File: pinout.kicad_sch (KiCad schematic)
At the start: 2 parts, among them J4 Conn_01x14_Pin, J6 Conn_01x14_Pin

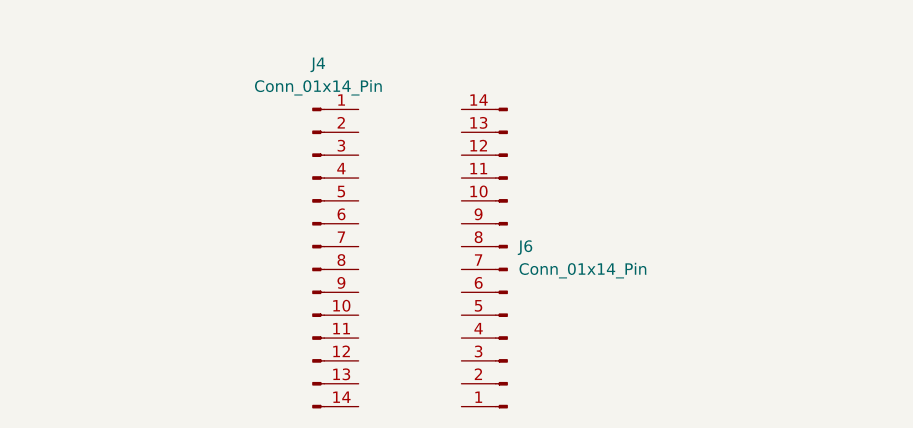
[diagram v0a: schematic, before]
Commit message: Added test Antenna
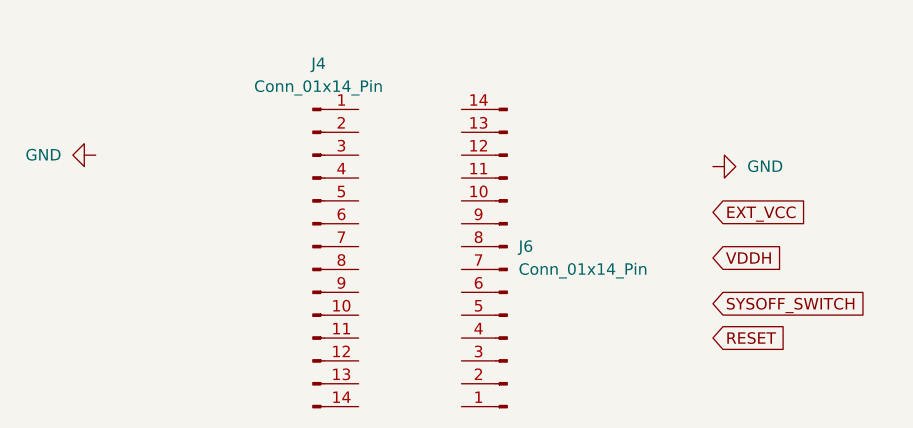
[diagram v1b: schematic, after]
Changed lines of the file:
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@@
 	(generator_version "9.0")
 	(paper "A4")
+	(global_label "EXT_VCC"
+		(shape input)
+		(at 157.48 96.52 0)
+		(fields_autoplaced yes)
+		(effects
+			(font
+				(size 1.27 1.27)
+			)
+			(justify left)
+		)
+		(property "Intersheetrefs" "${INTERSHEET_REFS}"
+			(at 168.3875 96.52 0)
+			(effects
+				(font
+					(size 1.27 1.27)
+				)
+				(justify left)
+				(hide yes)
+			)
+		)
+	)
+	(global_label "SYSOFF_SWITCH"
+		(shape input)
+		(at 157.48 106.68 0)
+		(fields_autoplaced yes)
+		(effects
+			(font
+				(size 1.27 1.27)
+			)
+			(justify left)
+		)
+		(property "Intersheetrefs" "${INTERSHEET_REFS}"
+			(at 175.2819 106.68 0)
+			(effects
+				(font
+					(size 1.27 1.27)
+				)
+				(justify left)
+				(hide yes)
+			)
+		)
+	)
+	(global_label "VDDH"
+		(shape input)
+		(at 157.48 101.6 0)
+		(fields_autoplaced yes)
+		(effects
+			(font
+				(size 1.27 1.27)
+			)
+			(justify left)
+		)
+		(property "Intersheetrefs" "${INTERSHEET_REFS}"
+			(at 165.4243 101.6 0)
+			(effects
+				(font
+					(size 1.27 1.27)
+				)
+				(justify left)
+				(hide yes)
+			)
+		)
+	)
+	(global_label "RESET"
+		(shape input)
+		(at 157.48 110.49 0)
+		(fields_autoplaced yes)
+		(effects
+			(font
+				(size 1.27 1.27)
+			)
+			(justify left)
+		)
+		(property "Intersheetrefs" "${INTERSHEET_REFS}"
+			(at 166.2103 110.49 0)
+			(effects
+				(font
+					(size 1.27 1.27)
+				)
+				(justify left)
+				(hide yes)
+			)
+		)
+	)
 	(symbol
 		(lib_id "Connector:Conn_01x14_Pin")
@@
 					(unit 1)
 				)
+			)
+		)
+	)
+	(symbol
+		(lib_id "power:GND")
+		(at 157.48 91.44 90)
+		(unit 1)
+		(exclude_from_sim no)
+		(in_bom yes)
+		(on_board yes)
+		(dnp no)
+		(fields_autoplaced yes)
+		(property "Reference" "#PWR038"
+			(at 163.83 91.44 0)
+			(effects
+				(font
+					(size 1.27 1.27)
+				)
+				(hide yes)
+			)
+		)
+		(property "Value" "GND"
+			(at 161.29 91.4399 90)
+			(effects
+				(font
+					(size 1.27 1.27)
+				)
+				(justify right)
+			)
+		)
+		(property "Footprint" ""
+			(at 157.48 91.44 0)
+			(effects
+				(font
+					(size 1.27 1.27)
+				)
+				(hide yes)
+			)
+		)
+		(property "Datasheet" ""
+			(at 157.48 91.44 0)
+			(effects
+				(font
+					(size 1.27 1.27)
+				)
+				(hide yes)
+			)
+		)
+		(property "Description" "Power symbol creates a global label with name \"GND\" , ground"
+			(at 157.48 91.44 0)
+			(effects
+				(font
+					(size 1.27 1.27)
+				)
+				(hide yes)
+			)
+		)
+		(pin "1"
+		)
+		(instances
+			(project "Slim Keyboard"
+				(path "/5d65a0d4-45a3-4af0-996a-c0381d04499a/f42a8a8a-4a34-440a-8e58-9c442fe0d23e/302a6436-4e3c-4497-ba91-0be99fe995f0"
+					(reference "#PWR038")
+					(unit 1)
+				)
+			)
+		)
+	)
+	(symbol
+		(lib_id "power:GND")
+		(at 88.9 90.17 270)
+		(unit 1)
+		(exclude_from_sim no)
+		(in_bom yes)
+		(on_board yes)
+		(dnp no)
+		(fields_autoplaced yes)
+		(property "Reference" "#PWR039"
+			(at 82.55 90.17 0)
+			(effects
+				(font
+					(size 1.27 1.27)
+				)
+				(hide yes)
+			)
+		)
+		(property "Value" "GND"
+			(at 85.09 90.1699 90)
+			(effects
+				(font
+					(size 1.27 1.27)
+				)
+				(justify right)
+			)
+		)
+		(property "Footprint" ""
+			(at 88.9 90.17 0)
+			(effects
+				(font
+					(size 1.27 1.27)
+				)
+				(hide yes)
+			)
+		)
+		(property "Datasheet" ""
+			(at 88.9 90.17 0)
+			(effects
+				(font
+					(size 1.27 1.27)
+				)
+				(hide yes)
+			)
+		)
+		(property "Description" "Power symbol creates a global label with name \"GND\" , ground"
+			(at 88.9 90.17 0)
+			(effects
+				(font
+					(size 1.27 1.27)
+				)
+				(hide yes)
+			)
+		)
+		(pin "1"
+		)
+		(instances
+			(project "Slim Keyboard"
+				(path "/5d65a0d4-45a3-4af0-996a-c0381d04499a/f42a8a8a-4a34-440a-8e58-9c442fe0d23e/302a6436-4e3c-4497-ba91-0be99fe995f0"
+					(reference "#PWR039")
+					(unit 1)
+				)

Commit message: Adjusted Footprint sizes
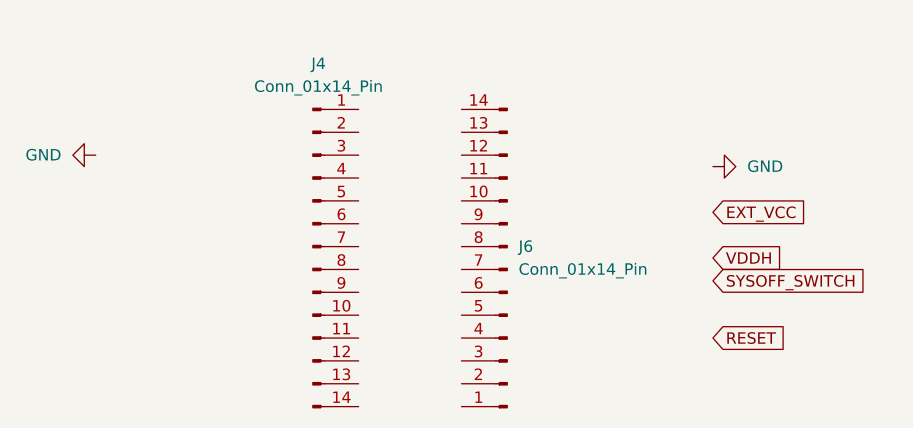
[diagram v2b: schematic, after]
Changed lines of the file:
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@@
 	(global_label "SYSOFF_SWITCH"
 		(shape input)
-		(at 157.48 106.68 0)
+		(at 157.48 104.14 0)
 		(fields_autoplaced yes)
 		(effects
@@
 		)
 		(property "Intersheetrefs" "${INTERSHEET_REFS}"
-			(at 175.2819 106.68 0)
+			(at 175.2819 104.14 0)
 			(effects
 				(font

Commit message: Started PCB design
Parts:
- removed J4, J6: Conn_01x14_Pin, Connector_PinHeader_2.54mm:PinHeader_1x14_P2.54mm_Vertical, symbol Connector:Conn_01x14_Pin
- added J7: ~, KBSlim_NRF52840_module:NRF52840_module, symbol KBSlim_NRF52840_module:NRF_Bluetooth_Module
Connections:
- net GND: now also J7.1, J7.28
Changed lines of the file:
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@@
 	(generator_version "9.0")
 	(paper "A4")
+	(wire
+		(pts
+			(xy 106.68 77.47) (xy 111.76 77.47)
+		)
+		(stroke
+			(width 0)
+			(type default)
+		)
+	)
+	(wire
+		(pts
+			(xy 132.08 77.47) (xy 137.16 77.47)
+		)
+		(stroke
+			(width 0)
+			(type default)
+		)
+	)
 	(global_label "EXT_VCC"
 		(shape input)
@@
 	)
 	(symbol
-		(lib_id "Connector:Conn_01x14_Pin")
-		(at 113.03 100.33 0)
+		(lib_id "power:GND")
+		(at 137.16 77.47 90)
 		(unit 1)
 		(exclude_from_sim no)
@@
 		(dnp no)
 		(fields_autoplaced yes)
-		(property "Reference" "J4"
-			(at 113.665 80.01 0)
-			(effects
-				(font
-					(size 1.27 1.27)
-				)
-			)
-		)
-		(property "Value" "Conn_01x14_Pin"
-			(at 113.665 82.55 0)
-			(effects
-				(font
-					(size 1.27 1.27)
-				)
-			)
-		)
-		(property "Footprint" "Connector_PinHeader_2.54mm:PinHeader_1x14_P2.54mm_Vertical"
-			(at 113.03 100.33 0)
-			(effects
-				(font
-					(size 1.27 1.27)
-				)
-				(hide yes)
-			)
-		)
-		(property "Datasheet" "~"
-			(at 113.03 100.33 0)
-			(effects
-				(font
-					(size 1.27 1.27)
-				)
-				(hide yes)
-			)
-		)
-		(property "Description" "Generic connector, single row, 01x14, script generated"
-			(at 113.03 100.33 0)
-			(effects
-				(font
-					(size 1.27 1.27)
-				)
-				(hide yes)
-			)
-		)
-		(pin "7"
-		)
-		(pin "2"
-		)
-		(pin "3"
-		)
-		(pin "6"
-		)
-		(pin "12"
-		)
-		(pin "4"
-		)
-		(pin "5"
-		)
-		(pin "9"
-		)
-		(pin "10"
+		(property "Reference" "#PWR038"
+			(at 143.51 77.47 0)
+			(effects
+				(font
+					(size 1.27 1.27)
+				)
+				(hide yes)
+			)
+		)
+		(property "Value" "GND"
+			(at 140.97 77.4699 90)
+			(effects
+				(font
+					(size 1.27 1.27)
+				)
+				(justify right)
+			)
+		)
+		(property "Footprint" ""
+			(at 137.16 77.47 0)
+			(effects
+				(font
+					(size 1.27 1.27)
+				)
+				(hide yes)
+			)
+		)
+		(property "Datasheet" ""
+			(at 137.16 77.47 0)
+			(effects
+				(font
+					(size 1.27 1.27)
+				)
+				(hide yes)
+			)
+		)
+		(property "Description" "Power symbol creates a global label with name \"GND\" , ground"
+			(at 137.16 77.47 0)
+			(effects
+				(font
+					(size 1.27 1.27)
+				)
+				(hide yes)
+			)
 		)
 		(pin "1"
 		)
-		(pin "11"
-		)
-		(pin "13"
-		)
-		(pin "8"
-		)
-		(pin "14"
-		)
 		(instances
-			(project ""
+			(project "Slim Keyboard"
 				(path "/5d65a0d4-45a3-4af0-996a-c0381d04499a/f42a8a8a-4a34-440a-8e58-9c442fe0d23e/302a6436-4e3c-4497-ba91-0be99fe995f0"
-					(reference "J4")
+					(reference "#PWR038")
 					(unit 1)
 				)
@@
 	)
 	(symbol
-		(lib_id "power:GND")
-		(at 157.48 91.44 90)
+		(lib_id "KBSlim_NRF52840_module:NRF_Bluetooth_Module")
+		(at 121.92 93.98 0)
 		(unit 1)
 		(exclude_from_sim no)
@@
 		(on_board yes)
 		(dnp no)
-		(fields_autoplaced yes)
-		(property "Reference" "#PWR038"
-			(at 163.83 91.44 0)
-			(effects
-				(font
-					(size 1.27 1.27)
-				)
-				(hide yes)
-			)
-		)
-		(property "Value" "GND"
-			(at 161.29 91.4399 90)
-			(effects
-				(font
-					(size 1.27 1.27)
-				)
-				(justify right)
-			)
-		)
-		(property "Footprint" ""
-			(at 157.48 91.44 0)
+		(property "Reference" "J7"
+			(at 120.65 93.98 0)
+			(effects
+				(font
+					(size 1.27 1.27)
+				)
+				(justify left)
+			)
+		)
+		(property "Value" "~"
+			(at 121.158 93.98 0)
+			(effects
+				(font
+					(size 1.27 1.27)
+				)
+				(justify left)
+				(hide yes)
+			)
+		)
+		(property "Footprint" "KBSlim_NRF52840_module:NRF52840_module"
+			(at 121.92 93.98 0)
 			(effects
 				(font
@@
 		)
 		(property "Datasheet" ""
-			(at 157.48 91.44 0)
-			(effects
-				(font
-					(size 1.27 1.27)
-				)
-				(hide yes)
-			)
-		)
-		(property "Description" "Power symbol creates a global label with name \"GND\" , ground"
-			(at 157.48 91.44 0)
-			(effects
-				(font
-					(size 1.27 1.27)
-				)
-				(hide yes)
-			)
+			(at 121.92 93.98 0)
+			(effects
+				(font
+					(size 1.27 1.27)
+				)
+				(hide yes)
+			)
+		)
+		(property "Description" ""
+			(at 121.92 93.98 0)
+			(effects
+				(font
+					(size 1.27 1.27)
+				)
+				(hide yes)
+			)
+		)
+		(pin "2"
 		)
 		(pin "1"
 		)
+		(pin "14"
+		)
+		(pin "25"
+		)
+		(pin "23"
+		)
+		(pin "21"
+		)
+		(pin "3"
+		)
+		(pin "7"
+		)
+		(pin "28"
+		)
+		(pin "27"
+		)
+		(pin "13"
+		)
+		(pin "4"
+		)
+		(pin "5"
+		)
+		(pin "6"
+		)
+		(pin "9"
+		)
+		(pin "10"
+		)
+		(pin "8"
+		)
+		(pin "11"
+		)
+		(pin "12"
+		)
+		(pin "26"
+		)
+		(pin "24"
+		)
+		(pin "22"
+		)
+		(pin "15"
+		)
+		(pin "20"
+		)
+		(pin "18"
+		)
+		(pin "16"
+		)
+		(pin "19"
+		)
+		(pin "17"
+		)
 		(instances
-			(project "Slim Keyboard"
+			(project ""
 				(path "/5d65a0d4-45a3-4af0-996a-c0381d04499a/f42a8a8a-4a34-440a-8e58-9c442fe0d23e/302a6436-4e3c-4497-ba91-0be99fe995f0"
-					(reference "#PWR038")
+					(reference "J7")
 					(unit 1)
 				)
@@
 	(symbol
 		(lib_id "power:GND")
-		(at 88.9 90.17 270)
+		(at 106.68 77.47 270)
 		(unit 1)
 		(exclude_from_sim no)
@@
 		(fields_autoplaced yes)
 		(property "Reference" "#PWR039"
-			(at 82.55 90.17 0)
+			(at 100.33 77.47 0)
 			(effects
 				(font
@@
 		)
 		(property "Value" "GND"
-			(at 85.09 90.1699 90)
+			(at 102.87 77.4699 90)
 			(effects
 				(font
@@
 		)
 		(property "Footprint" ""
-			(at 88.9 90.17 0)
+			(at 106.68 77.47 0)
 			(effects
 				(font
@@
 		)
 		(property "Datasheet" ""
-			(at 88.9 90.17 0)
+			(at 106.68 77.47 0)
 			(effects
 				(font
@@
 		)
 		(property "Description" "Power symbol creates a global label with name \"GND\" , ground"
-			(at 88.9 90.17 0)
+			(at 106.68 77.47 0)
 			(effects
 				(font
@@
 					(unit 1)
 				)
-			)
-		)
-	)
-	(symbol
-		(lib_id "Connector:Conn_01x14_Pin")
-		(at 134.62 102.87 180)
-		(unit 1)
-		(exclude_from_sim no)
-		(in_bom yes)
-		(on_board yes)
-		(dnp no)
-		(fields_autoplaced yes)
-		(property "Reference" "J6"
-			(at 135.89 100.3299 0)
-			(effects
-				(font
-					(size 1.27 1.27)
-				)
-				(justify right)
-			)
-		)
-		(property "Value" "Conn_01x14_Pin"
-			(at 135.89 102.8699 0)
-			(effects
-				(font
-					(size 1.27 1.27)
-				)
-				(justify right)
-			)
-		)
-		(property "Footprint" "Connector_PinHeader_2.54mm:PinHeader_1x14_P2.54mm_Vertical"
-			(at 134.62 102.87 0)
-			(effects
-				(font
-					(size 1.27 1.27)
-				)
-				(hide yes)
-			)
-		)
-		(property "Datasheet" "~"
-			(at 134.62 102.87 0)
-			(effects
-				(font
-					(size 1.27 1.27)
-				)
-				(hide yes)
-			)
-		)
-		(property "Description" "Generic connector, single row, 01x14, script generated"
-			(at 134.62 102.87 0)
-			(effects
-				(font
-					(size 1.27 1.27)
-				)
-				(hide yes)
-			)
-		)
-		(pin "7"
-		)
-		(pin "2"
-		)
-		(pin "3"
-		)
-		(pin "6"
-		)
-		(pin "12"
-		)
-		(pin "4"
-		)
-		(pin "5"
-		)
-		(pin "9"
-		)
-		(pin "10"
-		)
-		(pin "1"
-		)
-		(pin "11"
-		)
-		(pin "13"
-		)
-		(pin "8"
-		)
-		(pin "14"
-		)
-		(instances
-			(project "Slim Keyboard"
-				(path "/5d65a0d4-45a3-4af0-996a-c0381d04499a/f42a8a8a-4a34-440a-8e58-9c442fe0d23e/302a6436-4e3c-4497-ba91-0be99fe995f0"
-					(reference "J6")
-					(unit 1)
-				)

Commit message: Changed Pinout
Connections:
- net EXT_VCC: now also J7.2
- net GND: now also J7.25, J7.4
- net RESET: now also J7.3
- net SYSOFF_SWITCH: now also J7.26
- net VDDH: now also J7.27
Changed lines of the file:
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@@
+	(wire
+		(pts
+			(xy 106.68 85.09) (xy 111.76 85.09)
+		)
+		(stroke
+			(width 0)
+			(type default)
+		)
+	)
 	(wire
 		(pts
@@
 	(global_label "EXT_VCC"
 		(shape input)
-		(at 157.48 96.52 0)
+		(at 111.76 80.01 180)
 		(fields_autoplaced yes)
 		(effects
@@
 				(size 1.27 1.27)
 			)
-			(justify left)
+			(justify right)
 		)
 		(property "Intersheetrefs" "${INTERSHEET_REFS}"
-			(at 168.3875 96.52 0)
-			(effects
-				(font
-					(size 1.27 1.27)
-				)
-				(justify left)
+			(at 100.8525 80.01 0)
+			(effects
+				(font
+					(size 1.27 1.27)
+				)
+				(justify right)
 				(hide yes)
 			)
@@
 	(global_label "SYSOFF_SWITCH"
 		(shape input)
-		(at 157.48 104.14 0)
+		(at 132.08 82.55 0)
 		(fields_autoplaced yes)
 		(effects
@@
 		)
 		(property "Intersheetrefs" "${INTERSHEET_REFS}"
-			(at 175.2819 104.14 0)
+			(at 149.8819 82.55 0)
 			(effects
 				(font
@@
 	(global_label "VDDH"
 		(shape input)
-		(at 157.48 101.6 0)
+		(at 132.08 80.01 0)
 		(fields_autoplaced yes)
 		(effects
@@
 		)
 		(property "Intersheetrefs" "${INTERSHEET_REFS}"
-			(at 165.4243 101.6 0)
+			(at 140.0243 80.01 0)
 			(effects
 				(font
@@
 	(global_label "RESET"
 		(shape input)
-		(at 157.48 110.49 0)
+		(at 111.76 82.55 180)
 		(fields_autoplaced yes)
 		(effects
@@
 				(size 1.27 1.27)
 			)
-			(justify left)
+			(justify right)
 		)
 		(property "Intersheetrefs" "${INTERSHEET_REFS}"
-			(at 166.2103 110.49 0)
-			(effects
-				(font
-					(size 1.27 1.27)
-				)
-				(justify left)
+			(at 103.0297 82.55 0)
+			(effects
+				(font
+					(size 1.27 1.27)
+				)
+				(justify right)
 				(hide yes)
 			)
@@
 	(symbol
 		(lib_id "power:GND")
+		(at 106.68 85.09 270)
+		(unit 1)
+		(exclude_from_sim no)
+		(in_bom yes)
+		(on_board yes)
+		(dnp no)
+		(fields_autoplaced yes)
+		(property "Reference" "#PWR041"
+			(at 100.33 85.09 0)
+			(effects
+				(font
+					(size 1.27 1.27)
+				)
+				(hide yes)
+			)
+		)
+		(property "Value" "GND"
+			(at 102.87 85.0899 90)
+			(effects
+				(font
+					(size 1.27 1.27)
+				)
+				(justify right)
+			)
+		)
+		(property "Footprint" ""
+			(at 106.68 85.09 0)
+			(effects
+				(font
+					(size 1.27 1.27)
+				)
+				(hide yes)
+			)
+		)
+		(property "Datasheet" ""
+			(at 106.68 85.09 0)
+			(effects
+				(font
+					(size 1.27 1.27)
+				)
+				(hide yes)
+			)
+		)
+		(property "Description" "Power symbol creates a global label with name \"GND\" , ground"
+			(at 106.68 85.09 0)
+			(effects
+				(font
+					(size 1.27 1.27)
+				)
+				(hide yes)
+			)
+		)
+		(pin "1"
+		)
+		(instances
+			(project "Slim Keyboard"
+				(path "/5d65a0d4-45a3-4af0-996a-c0381d04499a/f42a8a8a-4a34-440a-8e58-9c442fe0d23e/302a6436-4e3c-4497-ba91-0be99fe995f0"
+					(reference "#PWR041")
+					(unit 1)
+				)
+			)
+		)
+	)
+	(symbol
+		(lib_id "power:GND")
 		(at 106.68 77.47 270)
 		(unit 1)
@@
 					(unit 1)
 				)
+			)
+		)
+	)
+	(symbol
+		(lib_id "power:GND")
+		(at 132.08 85.09 90)
+		(unit 1)
+		(exclude_from_sim no)
+		(in_bom yes)
+		(on_board yes)
+		(dnp no)
+		(fields_autoplaced yes)
+		(property "Reference" "#PWR042"
+			(at 138.43 85.09 0)
+			(effects
+				(font
+					(size 1.27 1.27)
+				)
+				(hide yes)
+			)
+		)
+		(property "Value" "GND"
+			(at 135.89 85.0899 90)
+			(effects
+				(font
+					(size 1.27 1.27)
+				)
+				(justify right)
+			)
+		)
+		(property "Footprint" ""
+			(at 132.08 85.09 0)
+			(effects
+				(font
+					(size 1.27 1.27)
+				)
+				(hide yes)
+			)
+		)
+		(property "Datasheet" ""
+			(at 132.08 85.09 0)
+			(effects
+				(font
+					(size 1.27 1.27)
+				)
+				(hide yes)
+			)
+		)
+		(property "Description" "Power symbol creates a global label with name \"GND\" , ground"
+			(at 132.08 85.09 0)
+			(effects
+				(font
+					(size 1.27 1.27)
+				)
+				(hide yes)
+			)
+		)
+		(pin "1"
+		)
+		(instances
+			(project "Slim Keyboard"
+				(path "/5d65a0d4-45a3-4af0-996a-c0381d04499a/f42a8a8a-4a34-440a-8e58-9c442fe0d23e/302a6436-4e3c-4497-ba91-0be99fe995f0"
+					(reference "#PWR042")
+					(unit 1)
+				)
